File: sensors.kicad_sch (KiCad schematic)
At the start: 4 parts, among them SW2 SW_DPST_x2

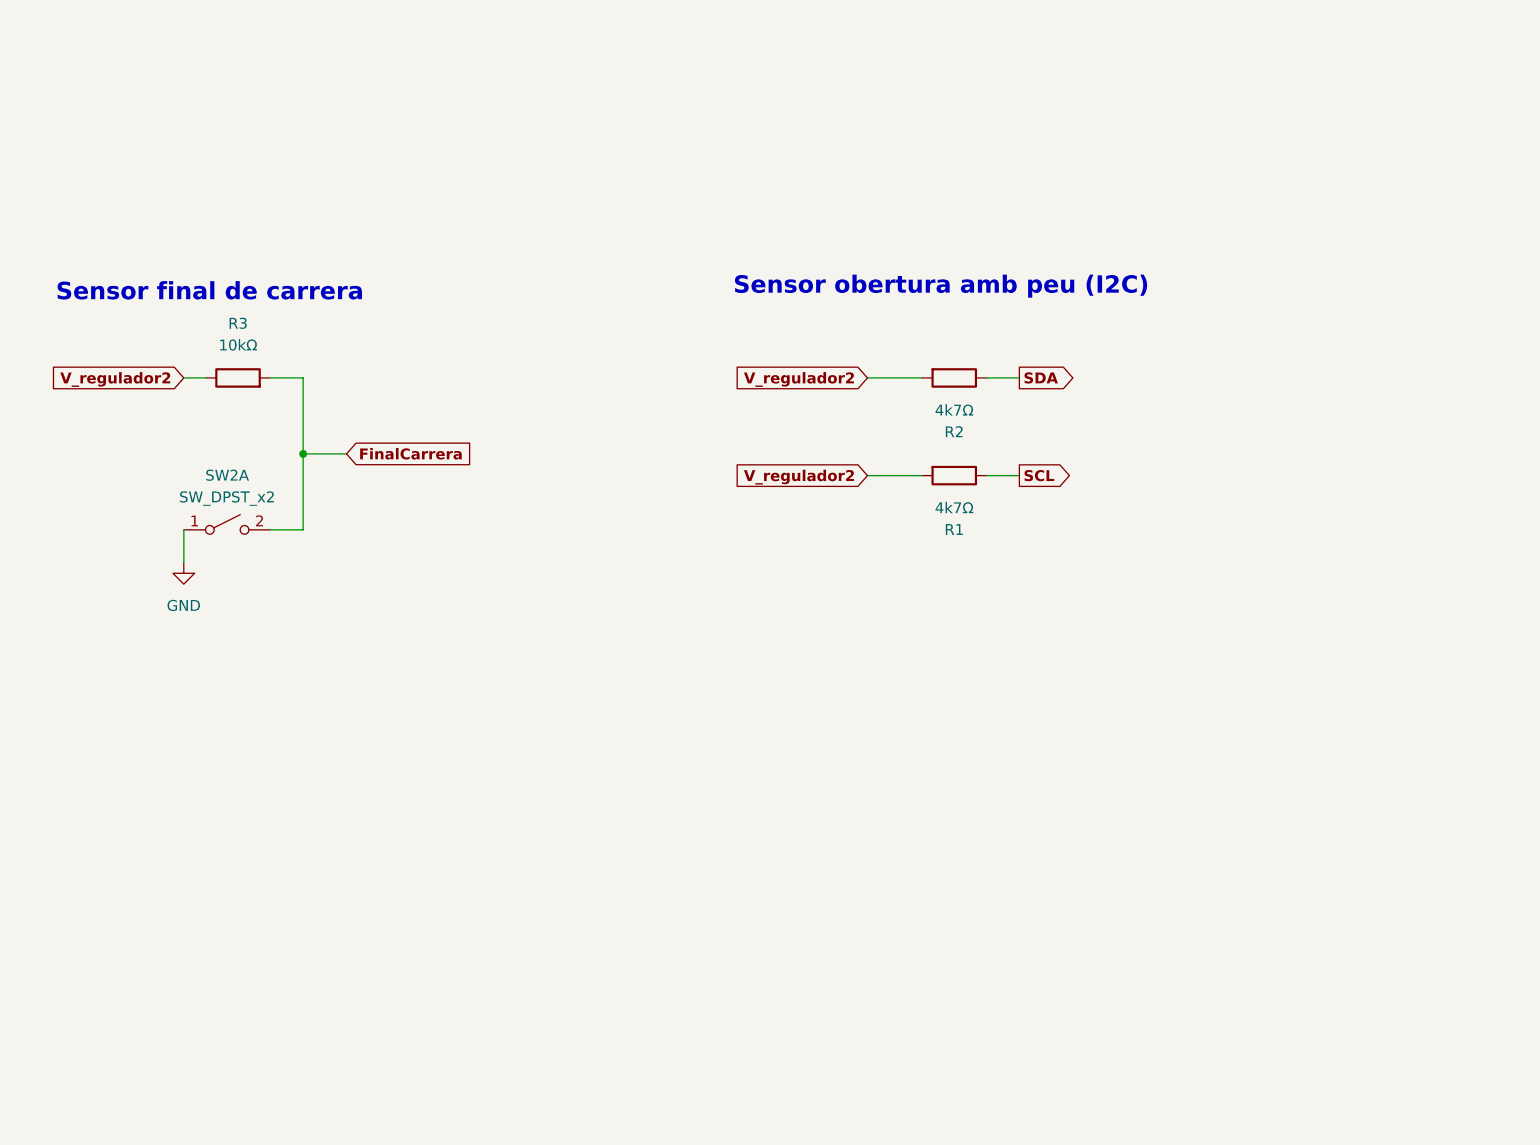
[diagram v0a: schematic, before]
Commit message: Actualització projecte KiCad
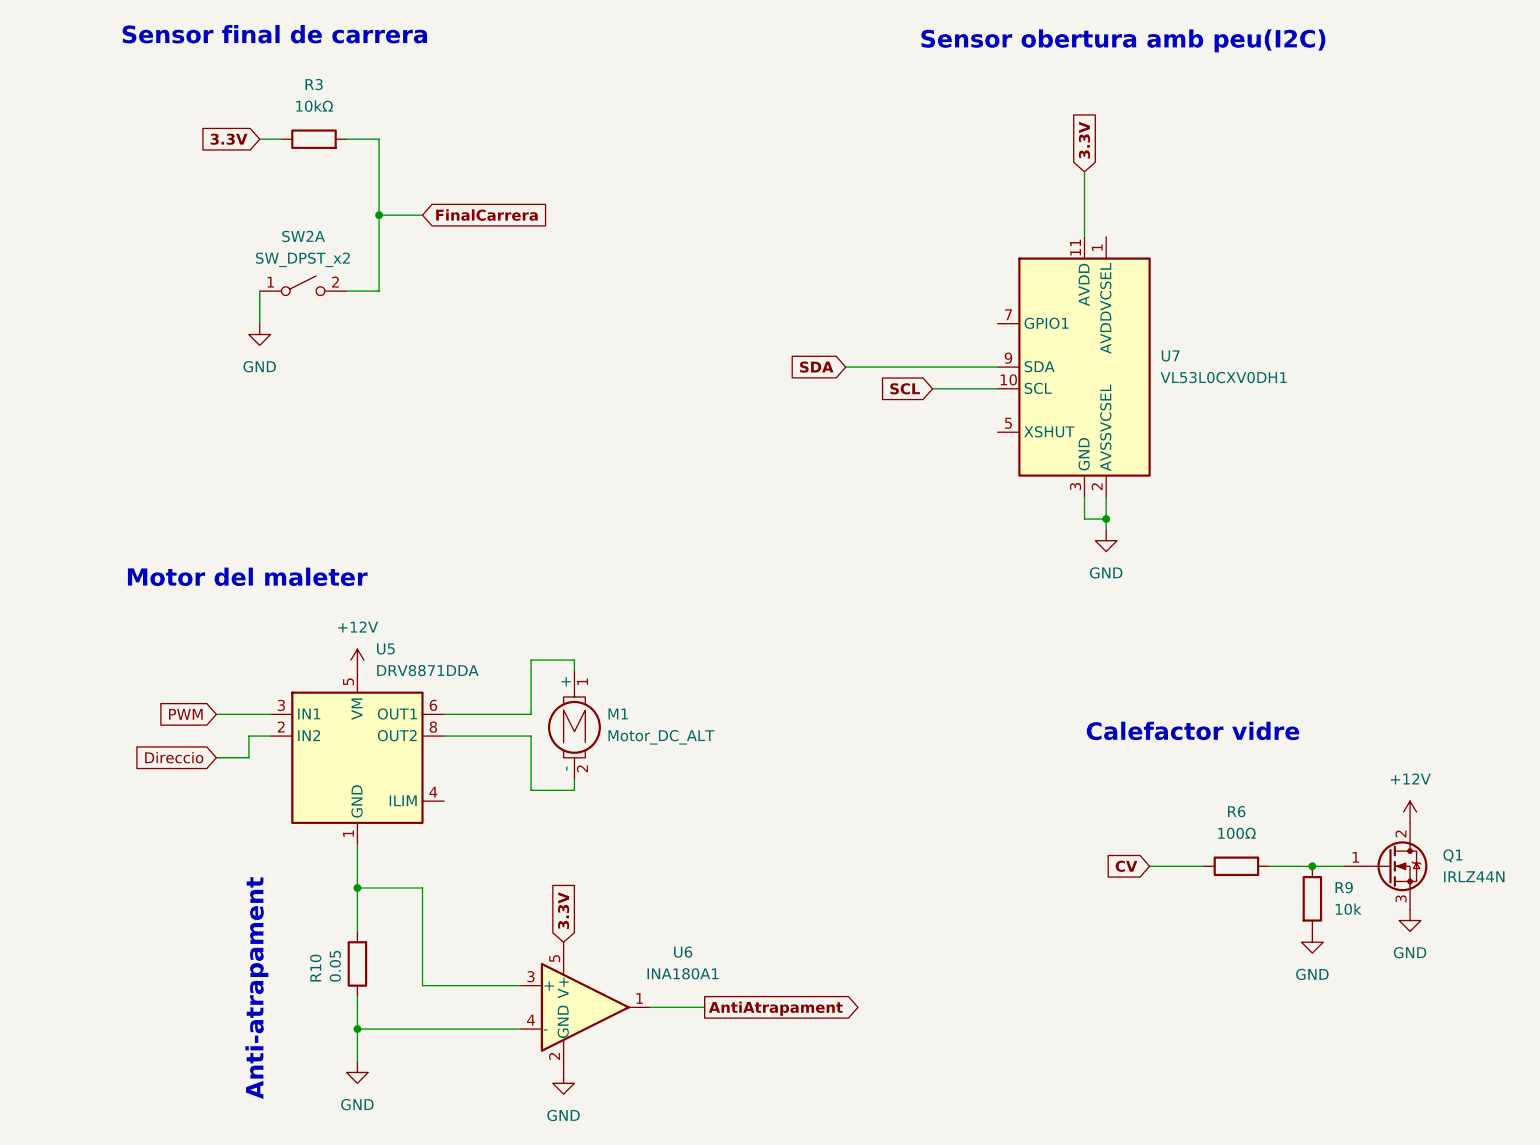
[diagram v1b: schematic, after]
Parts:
- removed R1, R2: 4k7Ω, symbol Device:R
- added M1: Motor_DC_ALT, symbol Motor:Motor_DC_ALT
- added Q1: IRLZ44N, Package_TO_SOT_THT:TO-220-3_Vertical, symbol Transistor_FET:IRLZ44N
- added R10: 0.05, symbol Device:R
- added R6: 100Ω, symbol Device:R
- added R9: 10k, symbol Device:R
- added U5: DRV8871DDA, Package_SO:Texas_HTSOP-8-1EP_3.9x4.9mm_P1.27mm_EP2.95x4.9mm_Mask2.4x3.1mm_ThermalVias, symbol Driver_Motor:DRV8871DDA
- added U6: INA180A1, Package_TO_SOT_SMD:SOT-23-5, symbol Amplifier_Current:INA180A1
- added U7: VL53L0CXV0DH1, Sensor_Distance:ST_VL53L1x, symbol Sensor_Distance:VL53L0CXV0DH1
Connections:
- net GND: now also Q1.3 (S), R10.1, R9.2, U6.2 (GND), U6.4 (-), U7.12 (GND), U7.2 (AVSSVCSEL), U7.3 (GND), U7.4 (GND), U7.6 (GND)
- net SCL: now also U7.10 (SCL)
- net SDA: now also U7.9 (SDA)
- net V_regulador2 renamed 3.3V
- net 3.3V: now also U6.5 (V+), U7.11 (AVDD)
- new net: R10.2, U5.1 (GND), U5.7 (GND), U5.9 (GND), U6.3 (+)
- new net: M1.1 (+), U5.6 (OUT1)
- new net: M1.2 (-), U5.8 (OUT2)
- new net: Q1.1 (G), R6.2, R9.1
- new net +12V: Q1.2 (D), U5.5 (VM)
- new net AntiAtrapament: U6.1
- new net CV: R6.1
- new net Direccio: U5.2 (IN2)
- new net PWM: U5.3 (IN1)
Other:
- note added: "Anti-atrapament"
- note added: "Calefactor vidre"
- note added: "Motor del maleter"
- note added: "Sensor obertura amb peu(I2C)"
- note removed: "Sensor obertura amb peu (I2C)"
- moved on the sheet: R3, SW2A
